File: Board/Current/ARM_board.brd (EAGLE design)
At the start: 101.6 x 81.3 mm, 171 parts, among them IC3 STM32F437VI, IC4 LM358DT, J1 USART/I2C, J10 ANALOG, J11 DGND, J12 DPWR, J13 DIGITAL, J14 SGND, J15 SPWR, J16 SERVO, J2 I2C2/USART3, J3 USART2, J5 SPI, J6 Bluesmirf, J7 SWD, J8 AGND, J9 APWR, Q1 STL4P2UH7, Q2 2STR1230, SW1 SW, U1 LSM330DLC, U10 BAV99, U11 BAV99, U12 USBLC6-2, U13 USBLC6-2, U14 STMPS2171MTR, U15 MC74HC164, U3 NC7SZU04, U4 L6206Q, U5 L6206Q, U6 SI7617, U7 SI7617, U8 SI7617, U9 SI7617, Y2 8MHz

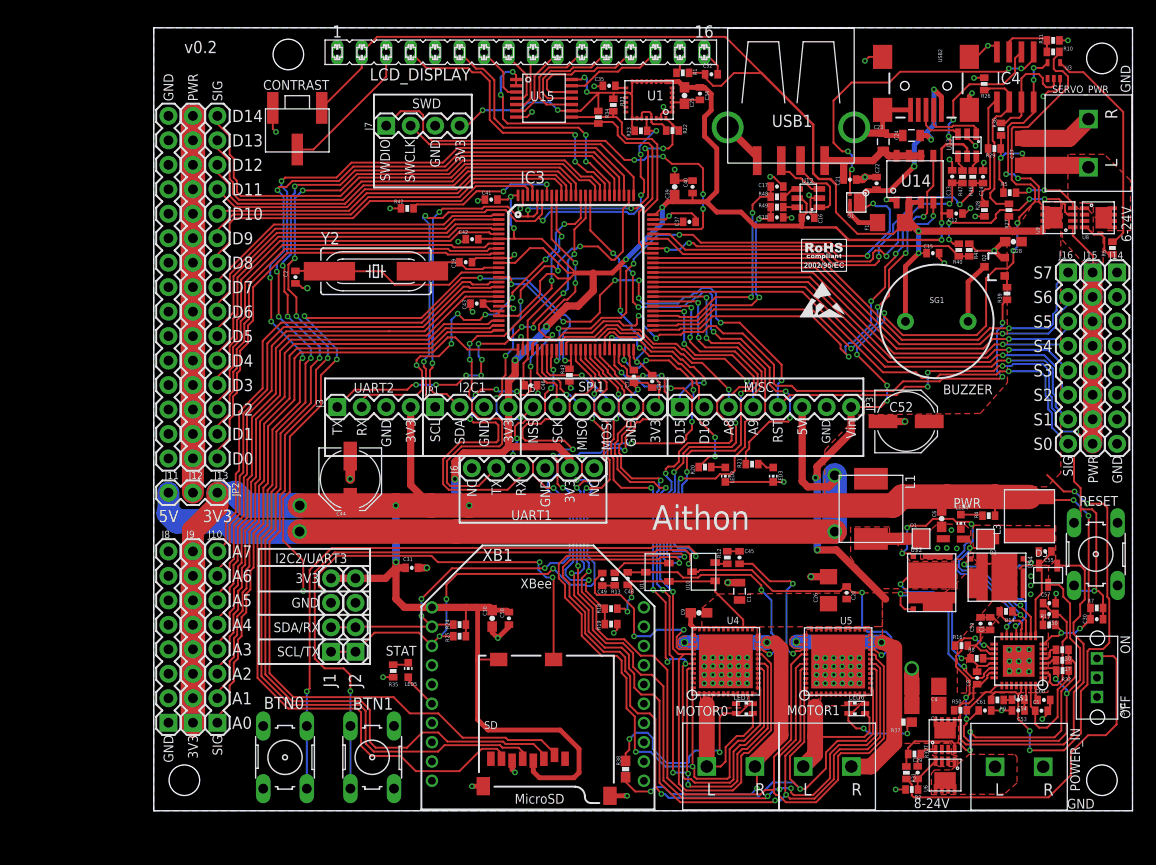
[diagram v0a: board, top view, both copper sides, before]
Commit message: Replaced LSM330DLC with LSM330 and re-added horse
LSM330 replaced LSM330DLC.
Re-added horse logo to board.
Moved labels in UART1 box down slightly.
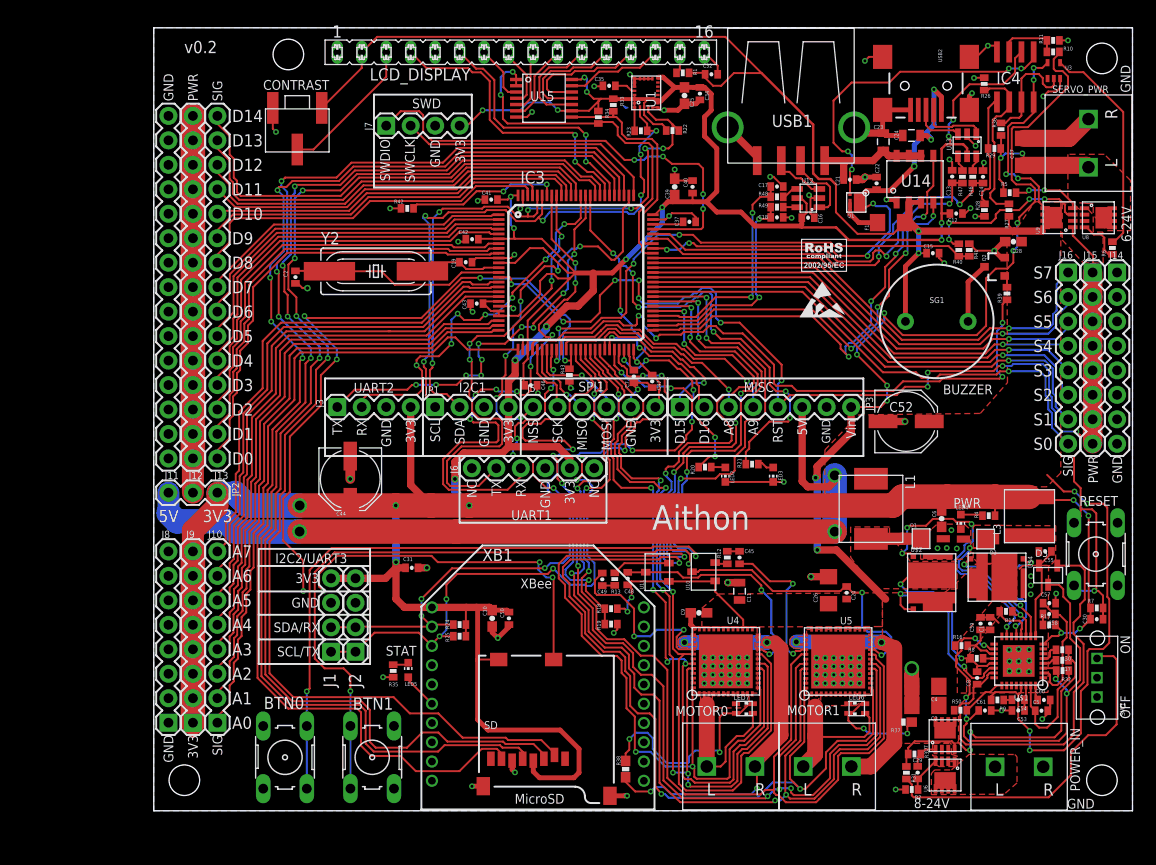
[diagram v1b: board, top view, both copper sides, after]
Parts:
- U1: value LSM330DLC -> LSM330; device r_cubed:LGA-28 -> r_cubed:LSM330
- moved U1 0.79 mm to (51.1, 74.5), turned to 90 degrees
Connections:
- net +3V3: now also U1.1, U1.24, U1.3; no longer U1.10, U1.11, U1.12, U1.14, U1.16, U1.21, U1.25, U1.9
- net GND: now also U1.14, U1.15, U1.16, U1.17, U1.18, U1.19, U1.20; no longer U1.1, U1.2, U1.26, U1.27, U1.3, U1.4
- net I2C1_SCL: now also U1.2; no longer U1.24
- net I2C1_SDA: now also U1.4; no longer U1.28
- net N$11: now also U1.21; no longer U1.15
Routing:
- net I2C1_SDA: track 61.3 -> 63.9 mm
- net GND: track 144.7 -> 147.0 mm, vias 117 -> 118
- net I2C1_SCL: track 59.2 -> 61.0 mm
- net N$11: track 1.16 -> 2.20 mm
- net +3V3: track 481.0 -> 482.0 mm
- net I2C2_SDA/USART3_RX: track 75.5 -> 76.1 mm

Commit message: Added 3.3V LDO for USB power to the schematic.
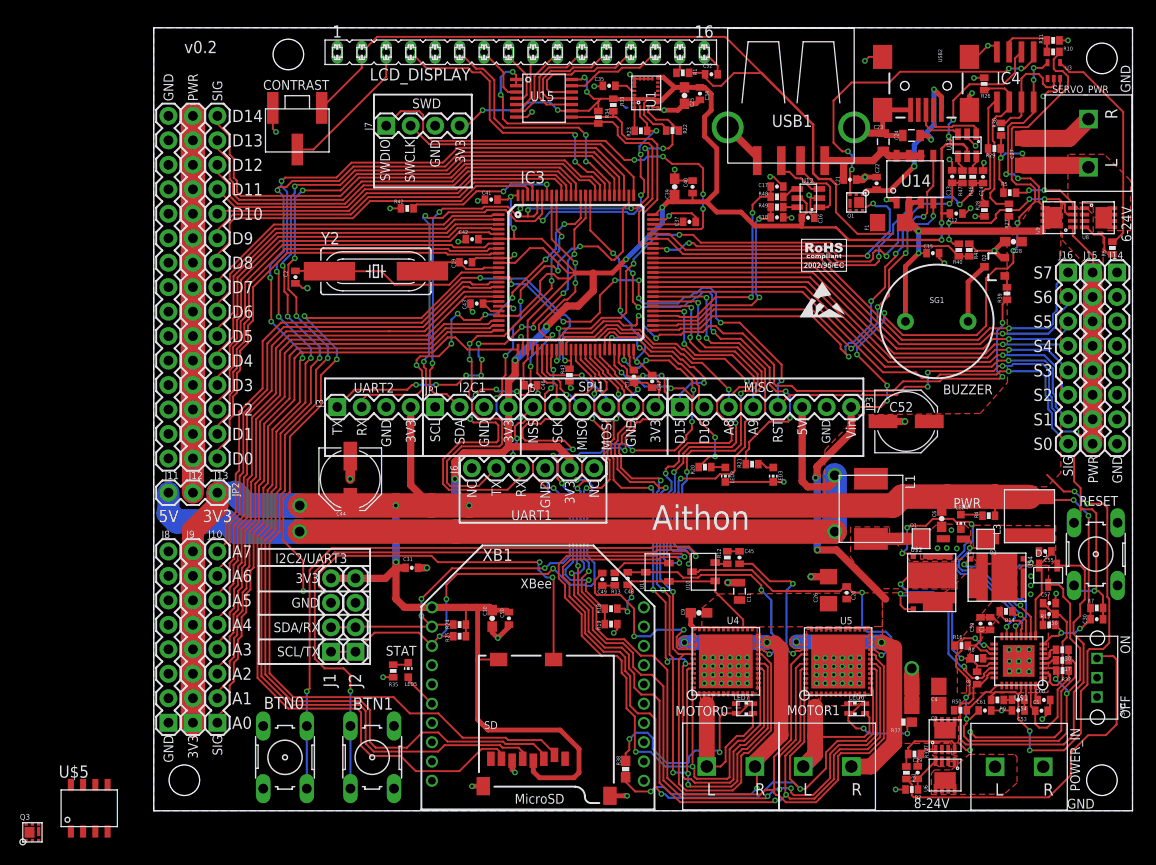
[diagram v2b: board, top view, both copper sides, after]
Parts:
- added Q3: STL4P2UH7, r_cubed:POWERFLAT
- added U$5: LD1117V33, r_cubed:8-SOIC
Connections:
- new net N$22: Q3.4, Q3.7, U$5.4
- net +3V3: now also U$5.2, U$5.3, U$5.6, U$5.7
- net 5V: now also Q1.4, Q1.7; no longer F1.2
- net GND: now also U$5.1
- net N$14: now also Q3.3
- net N$15: now also Q1.1, Q1.2, Q1.5, Q1.6, Q1.8, Q3.1, Q3.2, Q3.5, Q3.6, Q3.8; no longer Q1.4, Q1.7
- net USB_5V: now also F1.2; no longer Q1.1, Q1.2, Q1.5, Q1.6, Q1.8
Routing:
- net USB_5V: track 58.1 -> 51.6 mm
- net N$15: track 4.32 -> 0.00 mm
- net 5V: track 282.5 -> 279.9 mm

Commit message: Completed layout of new USB power parts.
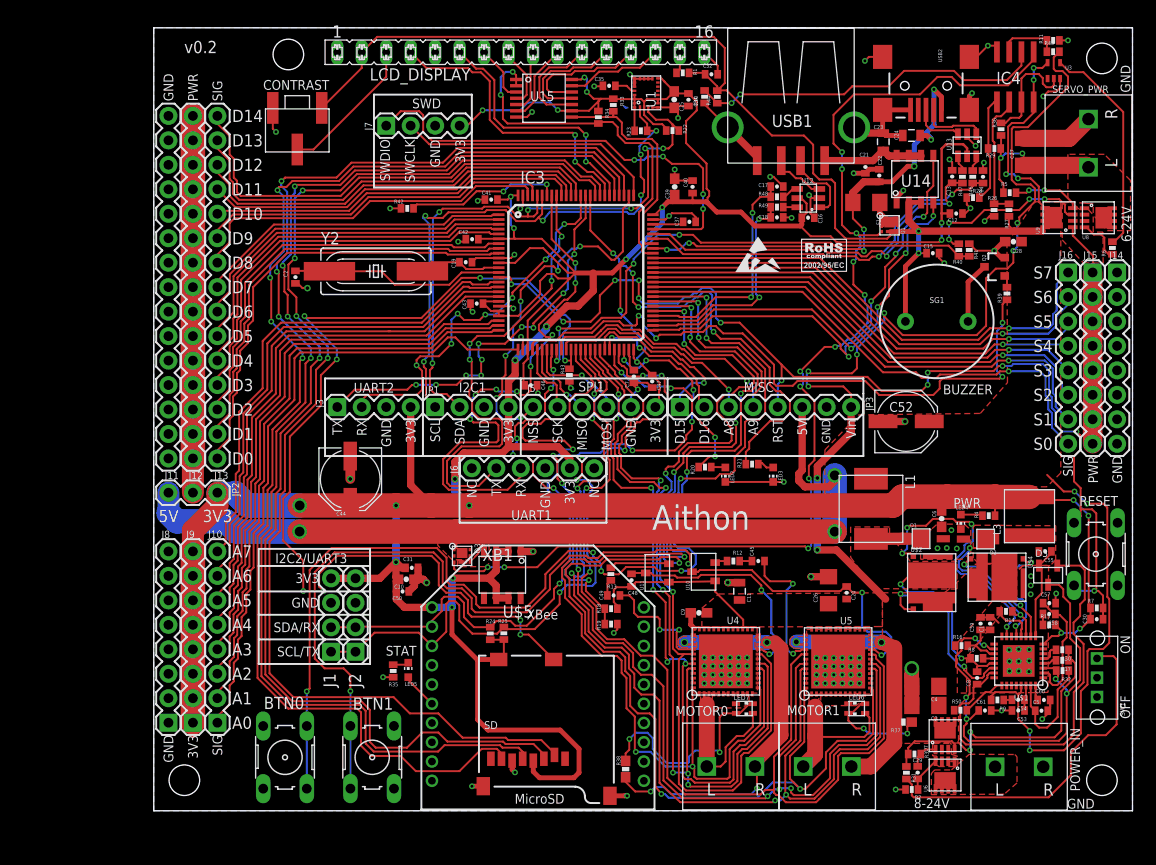
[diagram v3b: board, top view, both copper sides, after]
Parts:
- added R44, R45: 39k, SparkFun:0402-RES
- moved Q3 53.0 mm to (32.0, 26.5), turned to 270 degrees
- moved U$5 51.0 mm to (36.8, 25.1), turned to 180 degrees
- moved R10 36.5 mm to (57.2, 74.1), turned to 90 degrees
- moved R26 13.1 mm to (87.2, 62.4), turned to 90 degrees
- moved C50 11.4 mm to (25.8, 22.8), turned to 0 degrees
- moved C10 9.80 mm to (26.2, 24.0), turned to 0 degrees
- moved F1 4.81 mm to (74.0, 63.1), turned to 180 degrees
- moved R25 4.60 mm to (36.3, 18.4), turned to 270 degrees
- moved Q1 4.19 mm to (76.4, 60.8), turned to 270 degrees
- moved R24 3.31 mm to (34.9, 18.4), turned to 270 degrees
- moved C21 2.07 mm to (73.9, 66.8), turned to 270 degrees
- moved C49 2.05 mm to (47.7, 22.4), turned to 0 degrees
- moved C45 1.98 mm to (62.8, 25.9), turned to 0 degrees
- moved R28 1.76 mm to (85.0, 63.7), turned to 180 degrees
- moved C34 1.35 mm to (55.5, 73.8)
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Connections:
- removed net N$15: F1.1, Q1.1, Q1.2, Q1.5, Q1.6, Q1.8, Q3.1, Q3.2, Q3.5, Q3.6, Q3.8
- new net N$32: F1.1, Q1.1, Q1.2, Q1.5, Q1.6, Q1.8
- new net N$35: IC4.2, R10.2, R44.1
- net +3V3: no longer IC4.2
- net 5V: now also Q3.1, Q3.2, Q3.5, Q3.6, Q3.8, R44.2
- net GND: now also R10.1
- net N$5: now also R45.1; no longer R10.1
- net VIN: now also R45.2; no longer R10.2
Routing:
- net N$14: track 34.3 -> 119.1 mm, vias 4 -> 12
- net N$35: track 0.00 -> 37.3 mm, vias 0 -> 2
- net BTN0: track 108.6 -> 118.9 mm, vias 5 -> 7
- net BTN1: track 113.0 -> 121.3 mm
- net N$32: track 0.00 -> 7.87 mm
- net +3V3: track 482.0 -> 475.0 mm
- net N$45: track 19.4 -> 12.8 mm
- net GND: track 147.0 -> 152.6 mm, vias 118 -> 117
- net 5V: track 279.9 -> 284.4 mm
- net N$26: track 17.1 -> 13.2 mm
- net VIN: track 133.8 -> 137.5 mm, vias 12 -> 10
- net BOOT1: track 110.8 -> 108.3 mm
- net USB_DEV_DM: track 41.5 -> 39.6 mm
- net N$38: track 15.8 -> 14.2 mm
- net USB_5V: track 51.6 -> 50.2 mm
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- added copper zone on layer 1, net N$22

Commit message: Fixed the motor pins being swapped. Re-did a lot of the layout by the motors. Changed the big power traces that go through the center of the board to polygons.
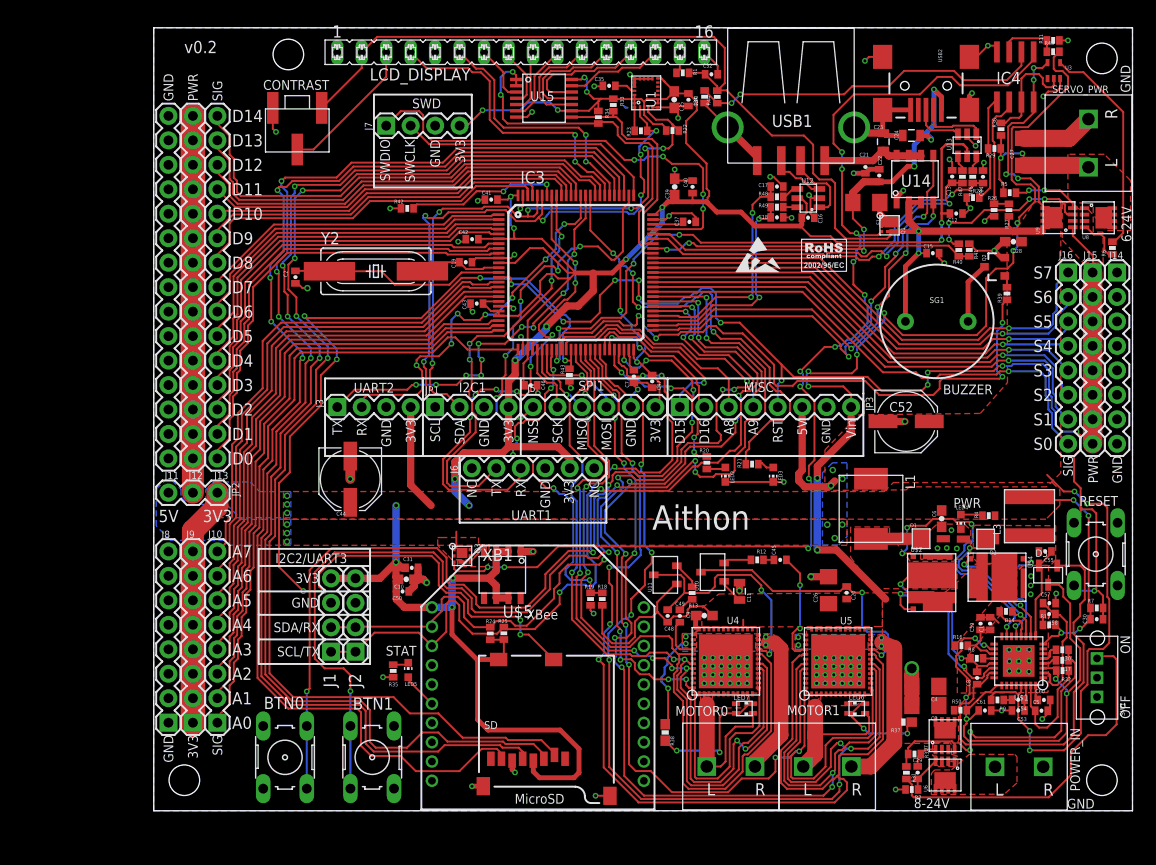
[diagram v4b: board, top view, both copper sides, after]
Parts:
- moved R13 8.67 mm to (55.9, 22.6)
- moved C49 7.19 mm to (54.6, 20.2), turned to 270 degrees
- moved R38 5.60 mm to (53.1, 8.13), turned to 270 degrees
- moved C48 5.28 mm to (53.3, 20.2)
- moved R19 3.36 mm to (45.3, 22.0), turned to 270 degrees
- moved R12 2.48 mm to (62.6, 26.0)
- moved C45 2.28 mm to (65.0, 26.0)
- moved R18 1.35 mm to (46.6, 22.0), turned to 90 degrees
- moved U10 0.93 mm to (58.0, 24.8)
- moved U11 0.85 mm to (53.1, 24.5)
- moved C9 0.63 mm to (57.1, 20.3)
- moved R20 0.49 mm to (57.4, 36.1), turned to 90 degrees
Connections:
- net M0_A: now also U4.17, U4.43; no longer U5.17, U5.43
- net M0_B: now also U4.18, U4.44; no longer U5.18, U5.44
- net M0_EN: now also U4.20, U4.41; no longer U5.20, U5.41
- net M0_FAULT: now also U4.13, U4.48; no longer U5.13, U5.48
- net M1_A: now also U5.17, U5.43; no longer U4.17, U4.43
- net M1_B: now also U5.18, U5.44; no longer U4.18, U4.44
- net M1_EN: now also U5.20, U5.41; no longer U4.20, U4.41
- net M1_FAULT: now also U5.13, U5.48; no longer U4.13, U4.48
- net OUT1: now also LED7.2, LED7.3, MOTOR0.L, U4.10, U4.11, U4.2, U4.3; no longer LED6.2, LED6.3, MOTOR1.L, U5.10, U5.11, U5.2, U5.3
- net OUT2: now also MOTOR0.R, R38.1, U4.22, U4.23, U4.38, U4.39; no longer MOTOR1.R, R37.1, U5.22, U5.23, U5.38, U5.39
- net OUT3: now also LED6.2, LED6.3, MOTOR1.L, U5.10, U5.11, U5.2, U5.3; no longer LED7.2, LED7.3, MOTOR0.L, U4.10, U4.11, U4.2, U4.3
- net OUT4: now also MOTOR1.R, R37.1, U5.22, U5.23, U5.38, U5.39; no longer MOTOR0.R, R38.1, U4.22, U4.23, U4.38, U4.39
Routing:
- net +3V3: track 475.0 -> 380.5 mm, vias 25 -> 27
- net 5V: track 284.4 -> 206.5 mm, vias 13 -> 19
- net M1_EN: track 76.9 -> 116.8 mm, vias 2 -> 4
- net M0_FAULT: track 130.4 -> 93.3 mm, vias 6 -> 10
- net M0_A: track 113.6 -> 77.3 mm, vias 7 -> 4
- net M1_A: track 72.5 -> 107.1 mm, vias 6 -> 8
- net M0_B: track 107.3 -> 79.2 mm, vias 6 -> 10
- net M0_EN: track 108.4 -> 81.4 mm
- net M1_B: track 85.7 -> 112.7 mm, vias 5 -> 7
- net OUT4: track 43.6 -> 19.1 mm
- net N$52: track 22.7 -> 13.8 mm
- net BTN0: track 118.9 -> 110.3 mm, vias 7 -> 5
- net N$45: track 12.8 -> 4.56 mm, vias 2 -> 0
- net VIN: track 137.5 -> 144.7 mm
- net M1_FAULT: track 111.4 -> 117.7 mm, vias 8 -> 10
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- added copper zone on layer 1, net +3V3
- added copper zone on layer 16, net +3V3
- added copper zone on layer 16, net 5V
- added copper zone on layer 16, net OUT2
- added copper zone on layer 16, net OUT4

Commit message: Switched Q3 around. Minor layout tweaks.
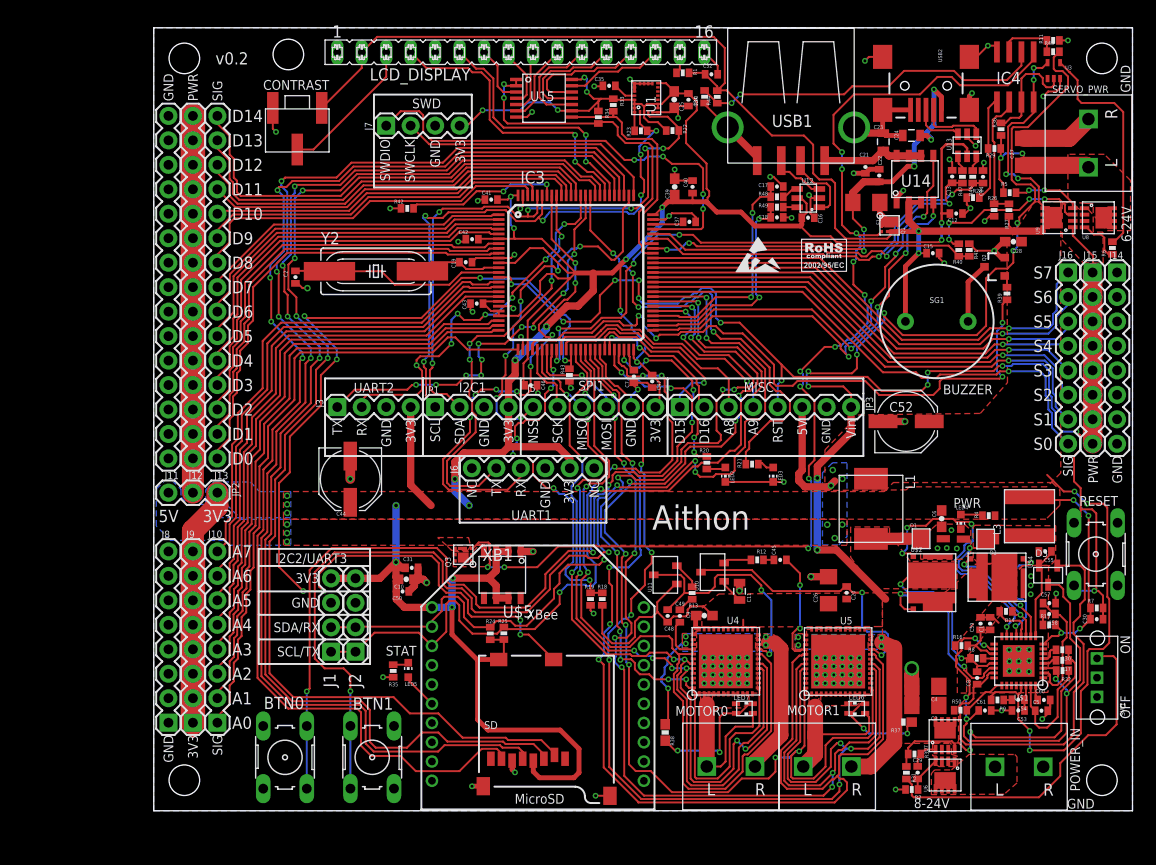
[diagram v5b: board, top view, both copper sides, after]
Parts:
- moved U1 0.50 mm to (51.1, 74.0)
- moved Q3 0.18 mm to (32.1, 26.6), turned to 90 degrees
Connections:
- net 5V: now also Q3.4, Q3.7; no longer Q3.1, Q3.2, Q3.5, Q3.6, Q3.8
- net N$22: now also Q3.1, Q3.2, Q3.5, Q3.6, Q3.8; no longer Q3.4, Q3.7
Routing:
- net 5V: track 206.5 -> 204.5 mm
- net LCD_DATA: track 37.6 -> 35.6 mm
- net N$30: track 22.7 -> 23.9 mm
- net +3V3: track 380.5 -> 379.6 mm
- net N$10: track 36.8 -> 36.2 mm
- net I2C1_SDA: track 63.9 -> 63.4 mm
- net I2C1_SCL: track 61.0 -> 60.5 mm
